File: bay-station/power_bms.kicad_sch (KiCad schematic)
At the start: 21 parts, among them J1 CUI PJ-063AH, J2 USB4125-GF-A, Q1 AO3401A, U1 MCP73871, U2 MAX17048G+T10

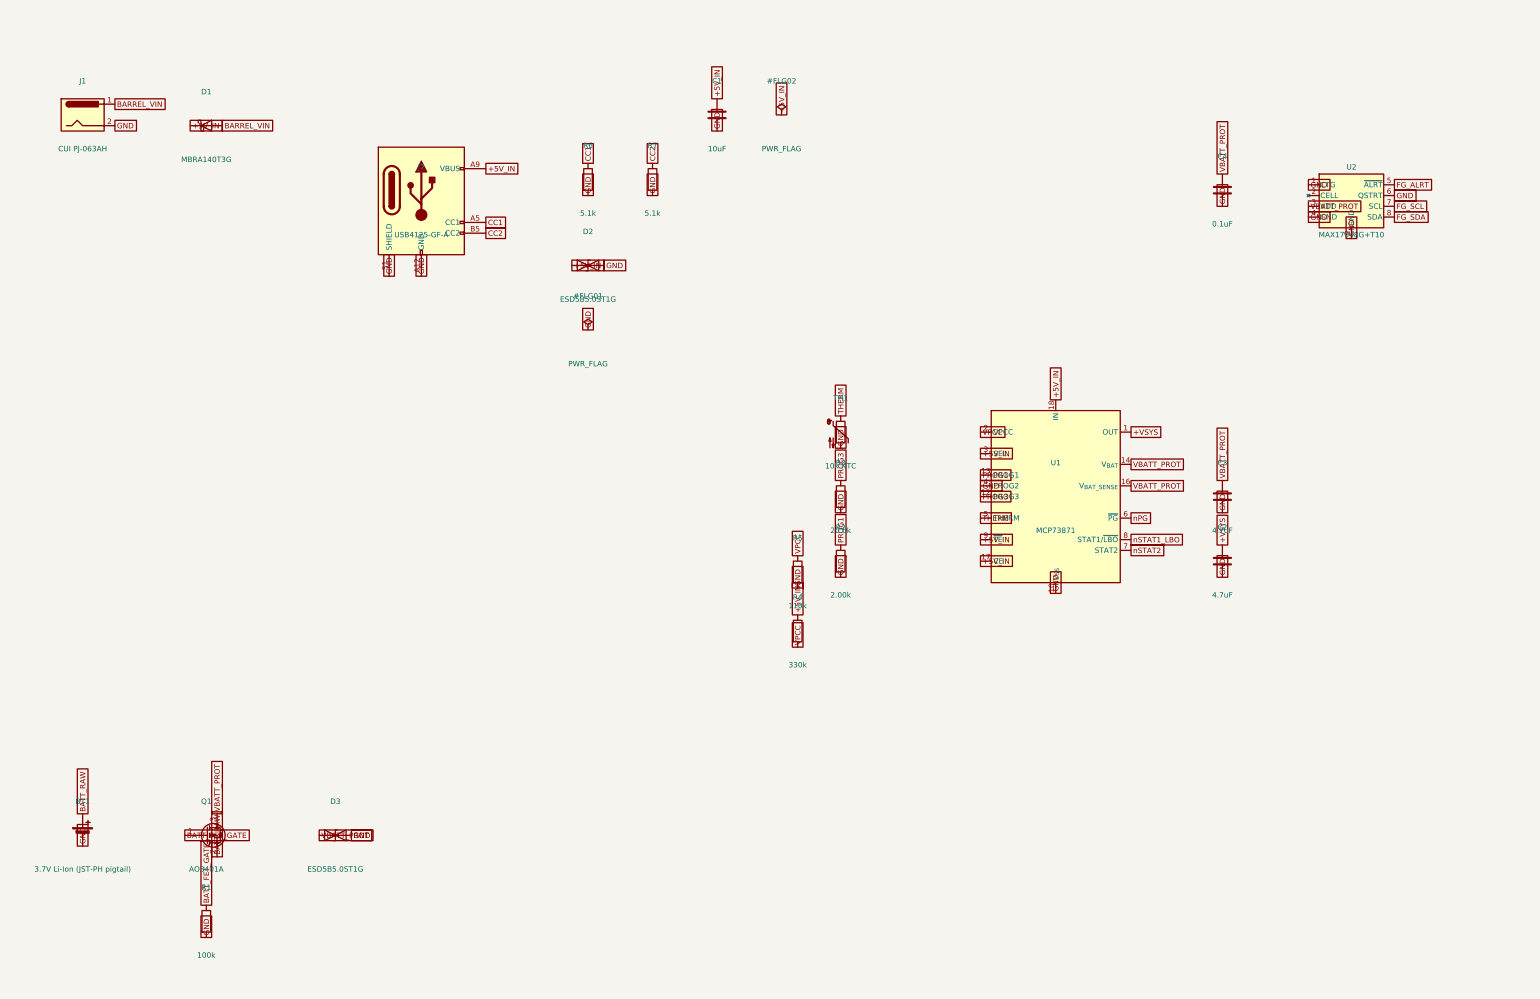
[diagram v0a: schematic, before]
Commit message: Wire up power_bms, regulation and programming_debug; tie off floating grounds
The bay station was built entirely from global labels and power symbols --
zero drawn wires on any sheet. This starts converting the power path to
explicit wiring and connects the grounds that were left floating:

- power_bms: 62 wires; 31 label justifications flipped left->right where
  the labels were mirrored. No symbols added or removed.
- regulation: 11 wires, 3 junctions, 5 GND symbols (#PWR01-05).
- programming_debug: 2 wires, 1 junction, 1 GND symbol (#PWR06).

ERC goes 518 -> 497 violations (494 -> 473 errors), entirely in
pin_not_connected (360 -> 342), power_pin_not_driven (98 -> 96) and
pin_not_driven (36 -> 35). Nothing regressed. The remaining 342
pin_not_connected are the sheets that are still label-only.

Unavoidable churn in this commit: KiCad 10 re-serialized seven sheets from
8.0 format (version 20231120) to 10.0 (20260306) on save -- clock_dist,
connectivity, gnss, indicators, programming_debug, testpoints, uwb_array.
That accounts for most of the diff; those seven have no content change
beyond it. CLAUDE.md asks that the format not be bumped as a side effect,
but it cannot be split out here: kicad-cli sch upgrade serializes
differently from the GUI and leaves ~3700 lines of residual churn, so a
format-only commit would be tidier in shape and no more honest. Four
sheets were already on 10.0 format before this commit.

Co-Authored-By: Claude Opus 5 (1M context) <noreply@anthropic.com>
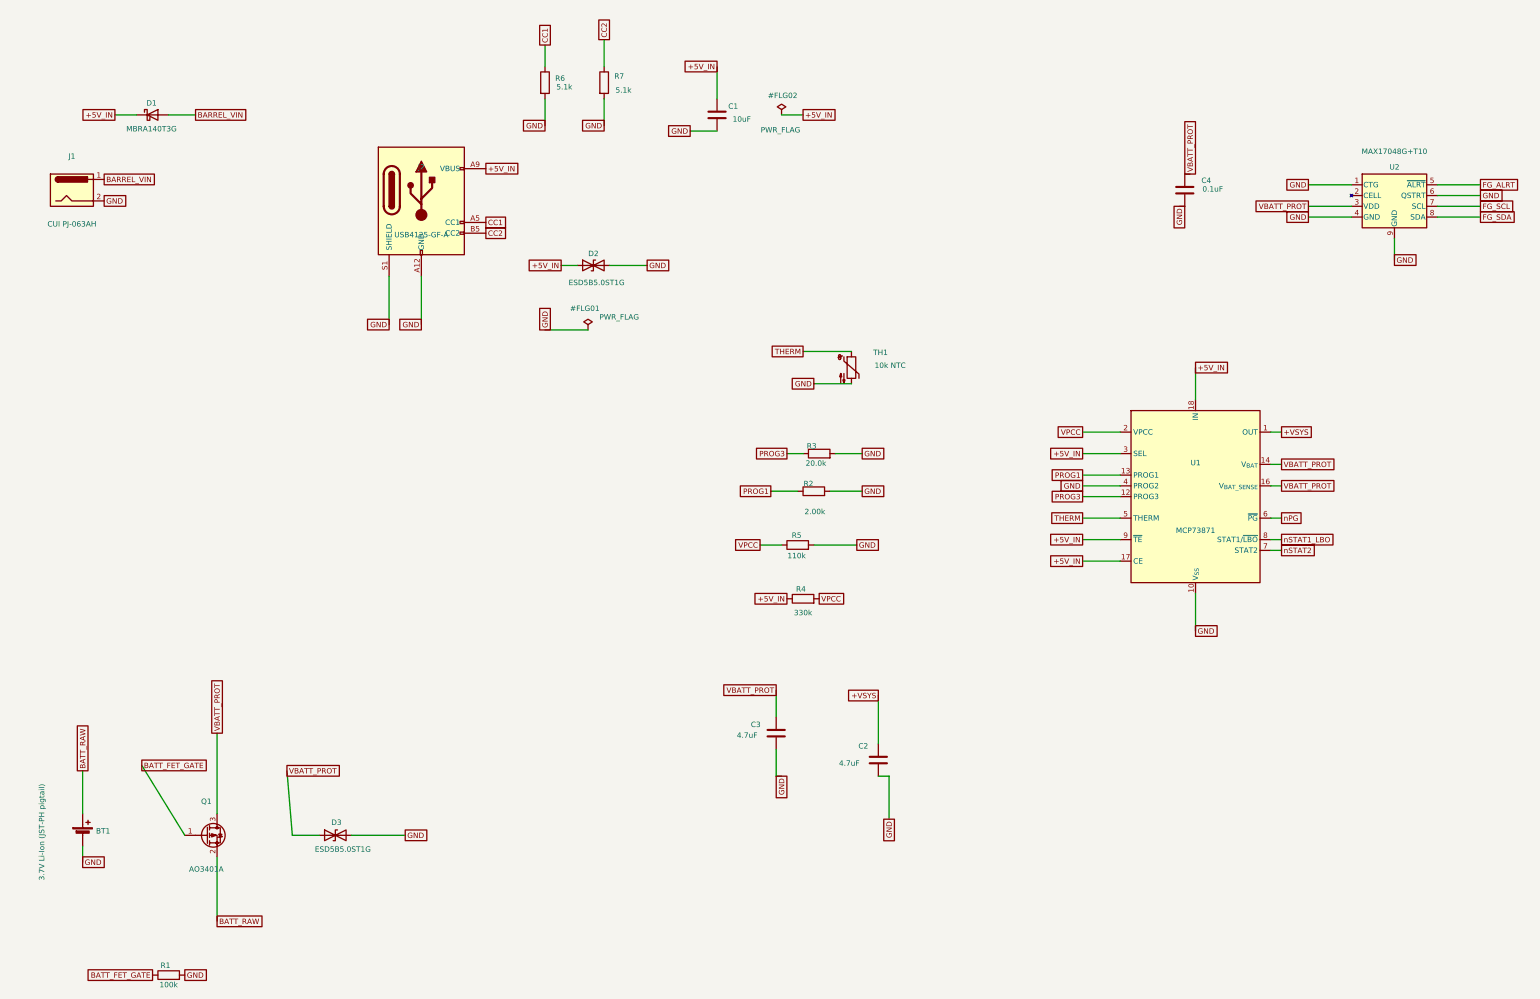
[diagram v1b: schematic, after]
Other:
- moved on the sheet: C2, C3, C4, D1, D2, J1, R1, R2, R3, R4, R5, R6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
